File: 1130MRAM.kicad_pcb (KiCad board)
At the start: 4 copper layers, 203.2 x 63.5 mm, 123 parts, among them J1 Screw_Terminal_01x03, J1A09 SLTpad, J1A11 SLTpad, K1E09 SLTpad, K1E11 SLTpad, M1A09 SLTpad, M1A11 SLTpad, M1C09 SLTpad, M1D09 SLTpad, M1E09 SLTpad, M1E11 SLTpad, Q1 IRF540N, SW1 SLTpad, U1 MR0A16AYS35, U10 74LCX38, U11 74LCX38, U12 SN74LVC1G123DCUR, U13 SN74LVC1G123DCUR, U14 74HC00, U15 74LS86, U16 74LS86, U17 74LS86, U18 74LS86, U2 SN74LV240APWR, U3 SN74LV240APWR, U4 LDL1117, U5 SN74LVC1G123DCUR, U6 SN74LVC1G123DCUR, U7 74LCX38, U8 74LCX38, U9 74LCX38

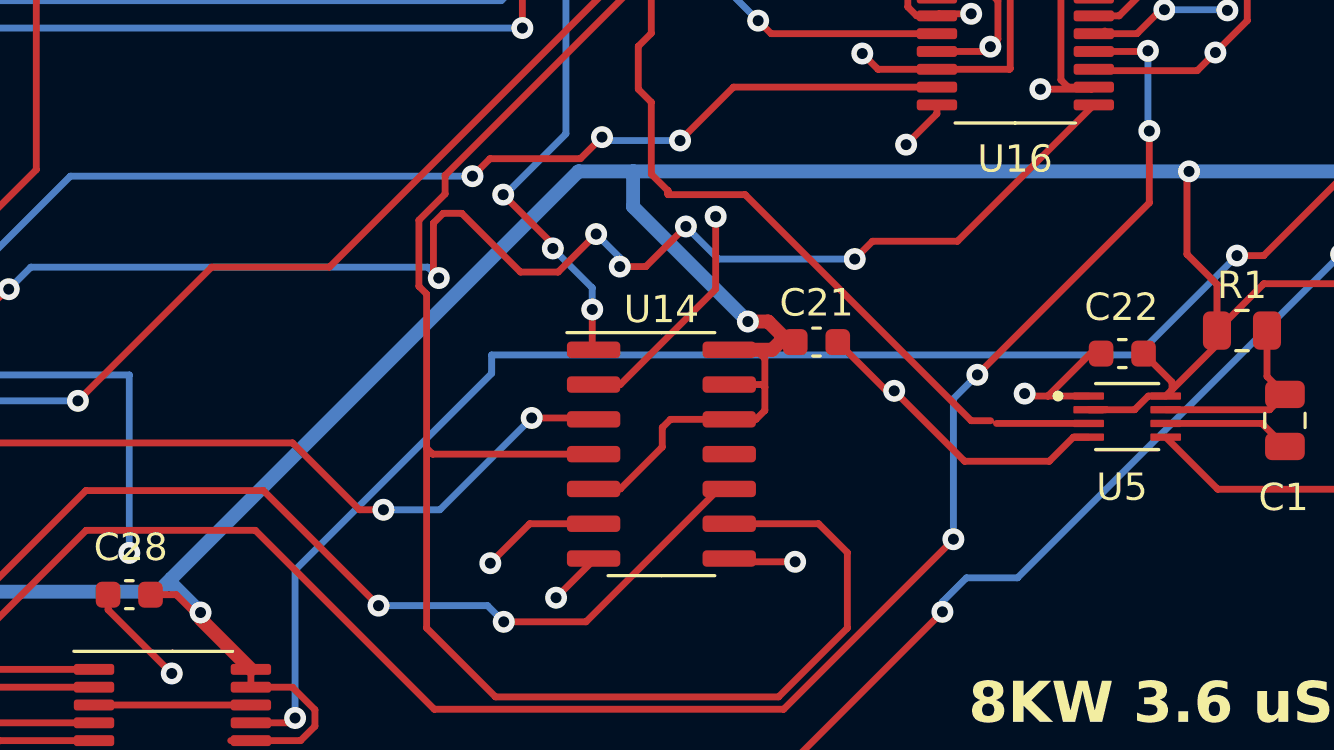
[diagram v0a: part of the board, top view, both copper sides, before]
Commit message: Corrected defect in design
Prior design optimization led to a failure mode that is experienced on the IBM 1130. Corrected the issue.
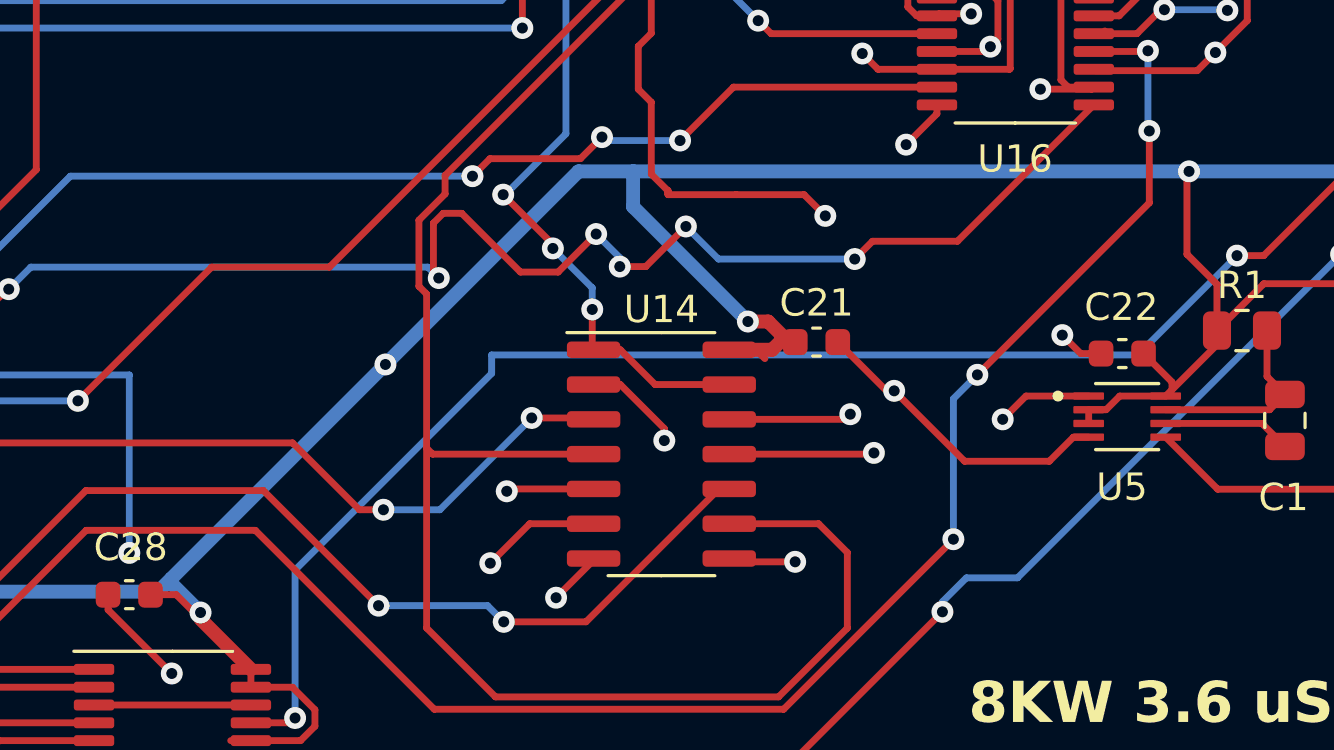
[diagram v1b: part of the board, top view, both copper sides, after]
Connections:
- U14 pad 11: unconnected-(U14-Pad11) -> Net-(U5-~{A})
- U14 pad 12: +3.3V -> Net-(SR1-Pin_1)
- U14 pad 13: +3.3V -> Net-(SU1-Pin_1)
- U5 pad 1: GND -> Net-(U5-~{A})
- U5 pad 3: Net-(SR1-Pin_1) -> +3.3V
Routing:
- net Net-(U5-~{A}): track 0.00 -> 14.0 mm, vias 0 -> 2
- net Net-(R10-Pad1): track 163.2 -> 151.7 mm
- net Net-(SU1-Pin_1): track 71.4 -> 76.9 mm
- net GND: track 147.5 -> 144.6 mm
- net +3.3V: track 598.9 -> 597.3 mm, vias 12 -> 14
- net Net-(SR1-Pin_1): track 75.9 -> 75.7 mm, vias 3 -> 5

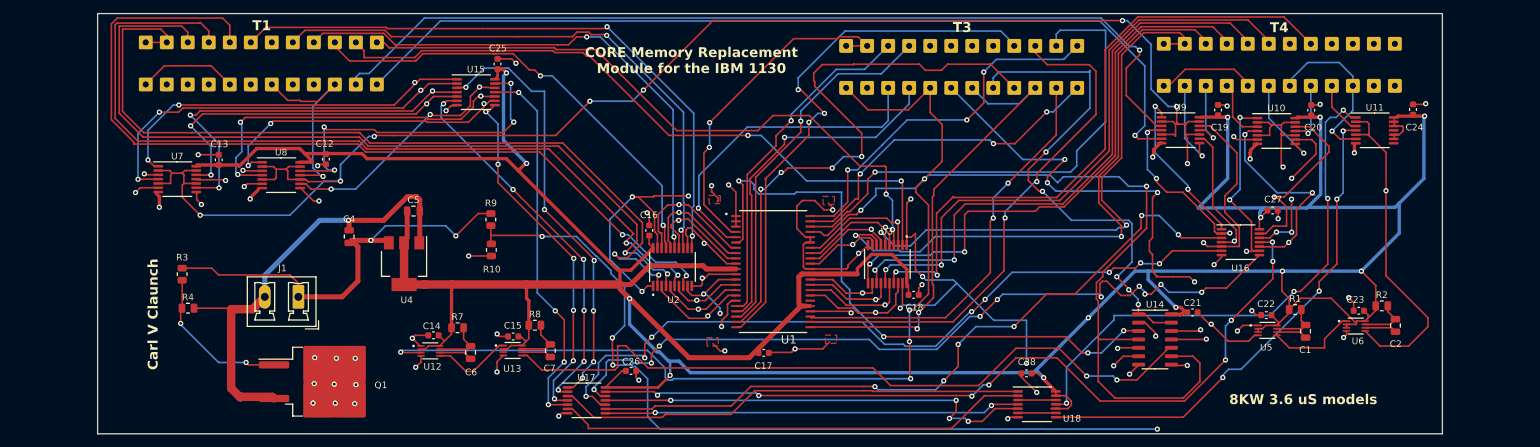
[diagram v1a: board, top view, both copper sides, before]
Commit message: Newest version of the PCB
based on testing with the 1130, the PCB was modified substantially
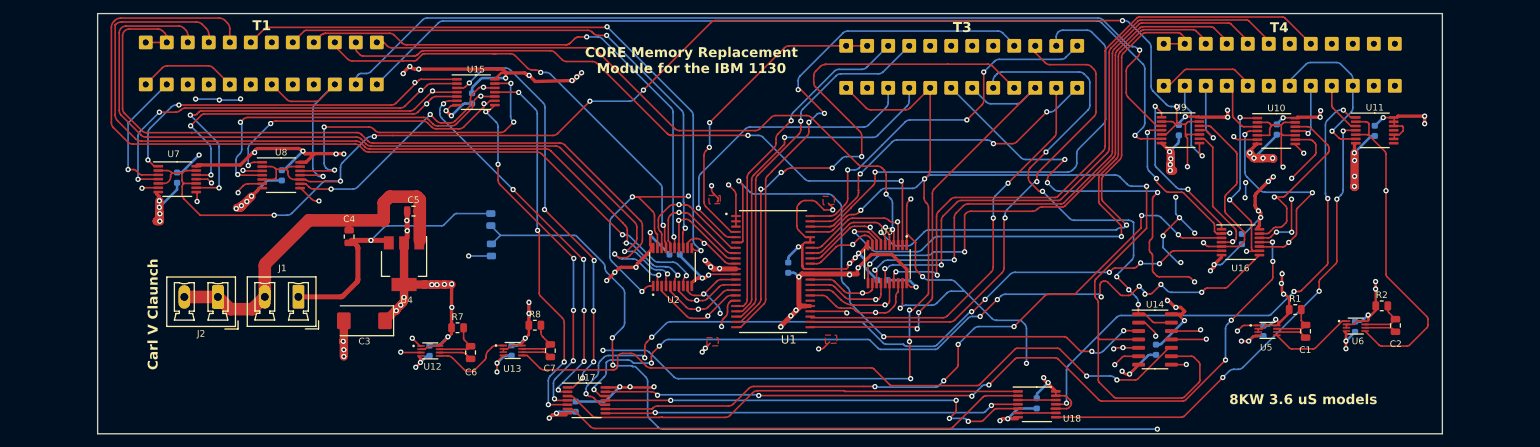
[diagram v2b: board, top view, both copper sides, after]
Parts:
- removed Q1: IRF540N, Package_TO_SOT_SMD:TO-263-2
- removed R3: 47k, Resistor_SMD:R_0805_2012Metric
- removed R4: 33k, Resistor_SMD:R_0805_2012Metric
- added C3: 470uF, Capacitor_Tantalum_SMD:CP_EIA-7343-30_AVX-N, F.Cu at (86.0, 102.3)
- added J2: Screw_Terminal_01x03, Connector_Phoenix_MC_HighVoltage:PhoenixContact_MCV_1,5_2-G-5.08_1x02_P5.08mm_Vertical, F.Cu at (63.9, 98.7)
- C12, C13, C14, C15, C16, C17, C18, C19, C20, C21, C22, C23, C24, C25, C26, C27, C28, R10, R9: moved to B.Cu
- moved C17 13.4 mm to (150.1, 94.3), turned to 90 degrees
- moved C26 9.96 mm to (118.0, 115.3), turned to -90 degrees
- moved C21 7.88 mm to (205.7, 106.7), turned to -90 degrees
- moved C12 7.10 mm to (73.5, 80.3)
- moved C13 6.85 mm to (57.7, 80.7), turned to -90 degrees
- moved C19 6.65 mm to (209.1, 73.5), turned to -90 degrees
- moved C24 6.62 mm to (238.7, 73.6), turned to -90 degrees
- moved C25 6.47 mm to (102.3, 68.7), turned to -90 degrees
- moved C27 6.35 mm to (218.6, 90.0), turned to 90 degrees
- moved C20 5.96 mm to (223.9, 73.4), turned to -90 degrees
- moved C16 5.27 mm to (132.9, 92.3), turned to 0 degrees
- moved C18 5.19 mm to (164.3, 96.2), turned to 180 degrees
- moved C28 4.78 mm to (187.6, 114.8), turned to 90 degrees
- moved C23 2.48 mm to (235.7, 103.2), turned to -90 degrees
- moved C22 2.42 mm to (221.9, 103.8), turned to -90 degrees
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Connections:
- net Net-(G1E11-Pin_1) renamed +SW
- C4 pad 2: /1130ground -> GND
- C5 pad 2: /1130ground -> GND
- J1 pad 2: /1130ground -> GND
- U4 pad 1: /1130ground -> GND
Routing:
- net +3.3V: track 597.3 -> 340.5 mm, vias 14 -> 81
- net GND: track 144.6 -> 251.7 mm, vias 47 -> 56
- net /1130ground: track 70.1 -> 0.00 mm, vias 1 -> 0
- net Net-(Q1-G): track 23.4 -> 0.00 mm, vias 2 -> 0
- net /+12V: track 64.4 -> 42.4 mm, vias 2 -> 1
- net +SW: track 267.8 -> 262.1 mm, vias 7 -> 8
- net Net-(G1E09-Pin_1): track 52.2 -> 47.7 mm
- net Net-(U1-DQL3): track 123.0 -> 119.0 mm
- net Net-(S0-Pin_1): track 17.0 -> 20.0 mm
- net Net-(U1-DQL4): track 110.4 -> 113.3 mm
- net Net-(U6-Q): track 332.0 -> 329.2 mm
- net Net-(S5-Pin_1): track 21.3 -> 24.0 mm
- net Net-(U13-Q): track 111.3 -> 108.9 mm
- net Net-(S1-Pin_1): track 23.3 -> 21.0 mm
- net Net-(U2-~{1OE}): track 145.1 -> 143.0 mm
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- added copper zone on In1.Cu, net +3.3V

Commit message: Changes after testing
tweaks to design, components, and documentation.
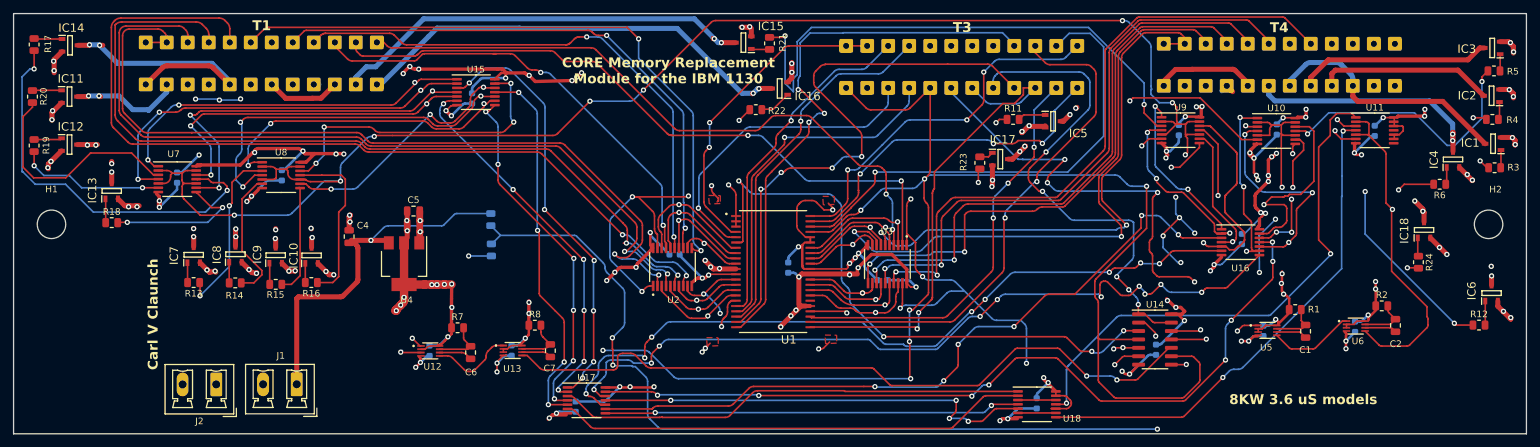
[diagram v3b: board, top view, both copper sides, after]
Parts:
- removed C3: 470uF, Capacitor_Tantalum_SMD:CP_EIA-7343-30_AVX-N
- added H1: MountingHole, MountingHole:MountingHole_4.3mm_M4, F.Cu at (38.8, 87.7)
- added H2: MountingHole, MountingHole:MountingHole_4.3mm_M4, F.Cu at (255.9, 87.7)
- added IC1: BSV52LT1G, SamacSys_Parts:SOT95P237X111-3N, F.Cu at (256.6, 75.5)
- added IC10: BSV52LT1G, SamacSys_Parts:SOT95P237X111-3N, F.Cu at (78.0, 92.4)
- added IC11: BSV52LT1G, SamacSys_Parts:SOT95P237X111-3N, F.Cu at (41.5, 68.4)
- added IC12: BSV52LT1G, SamacSys_Parts:SOT95P237X111-3N, F.Cu at (41.5, 75.7)
- added IC13: BSV52LT1G, SamacSys_Parts:SOT95P237X111-3N, F.Cu at (47.9, 82.7)
- added IC14: BSV52LT1G, SamacSys_Parts:SOT95P237X111-3N, F.Cu at (41.5, 60.7)
- added IC15: BSV52LT1G, SamacSys_Parts:SOT95P237X111-3N, F.Cu at (143.3, 60.3)
- added IC16: BSV52LT1G, SamacSys_Parts:SOT95P237X111-3N, F.Cu at (148.8, 67.2)
- added IC17: BSV52LT1G, SamacSys_Parts:SOT95P237X111-3N, F.Cu at (182.1, 77.9)
- added IC18: BSV52LT1G, SamacSys_Parts:SOT95P237X111-3N, F.Cu at (246.2, 88.6)
- added IC2: BSV52LT1G, SamacSys_Parts:SOT95P237X111-3N, F.Cu at (256.4, 68.3)
- added IC3: BSV52LT1G, SamacSys_Parts:SOT95P237X111-3N, F.Cu at (256.4, 61.1)
- added IC4: BSV52LT1G, SamacSys_Parts:SOT95P237X111-3N, F.Cu at (250.5, 77.9)
- added IC5: BSV52LT1G, SamacSys_Parts:SOT95P237X111-3N, F.Cu at (190.1, 72.2)
- added IC6: BSV52LT1G, SamacSys_Parts:SOT95P237X111-3N, F.Cu at (256.4, 98.1)
- added IC7: BSV52LT1G, SamacSys_Parts:SOT95P237X111-3N, F.Cu at (60.2, 92.3)
- added IC8: BSV52LT1G, SamacSys_Parts:SOT95P237X111-3N, F.Cu at (66.5, 92.2)
- added IC9: BSV52LT1G, SamacSys_Parts:SOT95P237X111-3N, F.Cu at (72.6, 92.4)
- added R11: 2k, Resistor_SMD:R_0805_2012Metric, F.Cu at (184.1, 71.9)
- added R12: 2K, Resistor_SMD:R_0805_2012Metric, F.Cu at (254.4, 103.0)
- added R13: 2K, Resistor_SMD:R_0805_2012Metric, F.Cu at (60.2, 96.5)
- added R14: 2k, Resistor_SMD:R_0805_2012Metric, F.Cu at (66.5, 96.6)
- added R15: 2k, Resistor_SMD:R_0805_2012Metric, F.Cu at (72.6, 96.8)
- added R16: 2k, Resistor_SMD:R_0805_2012Metric, F.Cu at (78.0, 96.5)
- added R17: 2k, Resistor_SMD:R_0805_2012Metric, F.Cu at (36.1, 60.6)
- added R18: 2k, Resistor_SMD:R_0805_2012Metric, F.Cu at (47.9, 87.5)
- added R19: 2k, Resistor_SMD:R_0805_2012Metric, F.Cu at (36.1, 75.8)
- added R20: 2k, Resistor_SMD:R_0805_2012Metric, F.Cu at (35.9, 68.4)
- added R21: 2k, Resistor_SMD:R_0805_2012Metric, F.Cu at (147.2, 60.4)
- added R22: 2k, Resistor_SMD:R_0805_2012Metric, F.Cu at (145.2, 70.4)
- added R23: 2k, Resistor_SMD:R_0805_2012Metric, F.Cu at (179.0, 78.4)
- added R24: 2k, Resistor_SMD:R_0805_2012Metric, F.Cu at (245.3, 93.5)
- added R3: 2k, Resistor_SMD:R_0805_2012Metric, F.Cu at (256.8, 79.2)
- added R4: 2k, Resistor_SMD:R_0805_2012Metric, F.Cu at (256.5, 71.9)
- added R5: 2k, Resistor_SMD:R_0805_2012Metric, F.Cu at (256.7, 64.5)
- added R6: 2k, Resistor_SMD:R_0805_2012Metric, F.Cu at (248.5, 81.7)
- U10, U11, U7, U8, U9: value 74LCX38 -> 74LVC08A
- U15, U16, U17, U18: value 74LS86 -> 74HC86
- moved J1 13.2 mm to (75.8, 111.9)
- moved J2 13.2 mm to (63.6, 111.9)
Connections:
- K1E11 pad 1: Net-(K1E11-Pin_1) -> Net-(IC5-C)
- M1A11 pad 1: Net-(M1A11-Pin_1) -> Net-(IC1-C)
- S0 pad 1: Net-(S0-Pin_1) -> Net-(IC11-C)
- S1 pad 1: Net-(S1-Pin_1) -> Net-(IC12-C)
- S10 pad 1: Net-(S10-Pin_1) -> Net-(IC17-C)
- S11 pad 1: Net-(S11-Pin_1) -> Net-(IC18-C)
- S12 pad 1: Net-(S12-Pin_1) -> Net-(IC6-C)
- S13 pad 1: Net-(K1E11-Pin_1) -> Net-(IC5-C)
- S14 pad 1: Net-(S14-Pin_1) -> Net-(IC4-C)
- S15 pad 1: Net-(S15-Pin_1) -> Net-(IC3-C)
- S16 pad 1: Net-(S16-Pin_1) -> Net-(IC2-C)
- S17 pad 1: Net-(M1A11-Pin_1) -> Net-(IC1-C)
- S2 pad 1: Net-(S2-Pin_1) -> Net-(IC13-C)
- S4 pad 1: Net-(S4-Pin_1) -> Net-(IC7-C)
- S5 pad 1: Net-(S5-Pin_1) -> Net-(IC8-C)
- S6 pad 1: Net-(S6-Pin_1) -> Net-(IC9-C)
- S8 pad 1: Net-(S8-Pin_1) -> Net-(IC15-C)
- S9 pad 1: Net-(S9-Pin_1) -> Net-(IC16-C)
- U10 pad 11: Net-(S15-Pin_1) -> Net-(R5-Pad2)
- U10 pad 3: Net-(S12-Pin_1) -> Net-(R12-Pad1)
- U10 pad 6: Net-(K1E11-Pin_1) -> Net-(R11-Pad1)
- U10 pad 8: Net-(S14-Pin_1) -> Net-(R6-Pad2)
- U11 pad 3: Net-(S16-Pin_1) -> Net-(R4-Pad1)
- U11 pad 6: Net-(M1A11-Pin_1) -> Net-(R3-Pad1)
- U7 pad 11: Net-(A1E11-Pin_1) -> Net-(R17-Pad2)
- U7 pad 3: Net-(S0-Pin_1) -> Net-(R20-Pad2)
- U7 pad 6: Net-(S1-Pin_1) -> Net-(R19-Pad2)
- U7 pad 8: Net-(S2-Pin_1) -> Net-(R18-Pad2)
- U8 pad 11: Net-(C1A11-Pin_1) -> Net-(R16-Pad1)
- U8 pad 3: Net-(S4-Pin_1) -> Net-(R13-Pad1)
- U8 pad 6: Net-(S5-Pin_1) -> Net-(R14-Pad1)
- U8 pad 8: Net-(S6-Pin_1) -> Net-(R15-Pad2)
- U9 pad 11: Net-(S11-Pin_1) -> Net-(R24-Pad2)
- U9 pad 3: Net-(S8-Pin_1) -> Net-(R21-Pad2)
- U9 pad 6: Net-(S9-Pin_1) -> Net-(R22-Pad2)
- U9 pad 8: Net-(S10-Pin_1) -> Net-(R23-Pad2)
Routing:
- net Net-(S8-Pin_1): track 139.8 -> 0.00 mm, vias 1 -> 0
- net Net-(S9-Pin_1): track 137.9 -> 0.00 mm, vias 1 -> 0
- net Net-(R21-Pad2): track 0.00 -> 84.7 mm, vias 0 -> 2
- net Net-(R22-Pad2): track 0.00 -> 71.2 mm, vias 0 -> 2
- net Net-(IC16-C): track 0.00 -> 67.7 mm, vias 0 -> 2
- net Net-(IC15-C): track 0.00 -> 63.8 mm, vias 0 -> 2
- net Net-(R17-Pad2): track 0.00 -> 60.3 mm, vias 0 -> 2
- net Net-(IC6-C): track 0.00 -> 59.5 mm, vias 0 -> 2
- net Net-(R12-Pad1): track 0.00 -> 52.9 mm, vias 0 -> 3
- net Net-(IC18-C): track 0.00 -> 47.7 mm, vias 0 -> 2
- net Net-(R11-Pad1): track 0.00 -> 46.5 mm, vias 0 -> 2
- net Net-(R24-Pad2): track 0.00 -> 46.3 mm, vias 0 -> 2
- net Net-(R5-Pad2): track 0.00 -> 41.3 mm, vias 0 -> 2
- net Net-(IC1-C): track 0.00 -> 38.6 mm
- net Net-(IC4-C): track 0.00 -> 38.5 mm, vias 0 -> 2
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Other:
- board size 203.2 x 63.5 mm -> 228.6 x 63.5 mm
